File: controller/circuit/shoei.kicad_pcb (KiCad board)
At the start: 2 copper layers, 68.6 x 53.3 mm, 28 parts, among them J1 LED1, J2 LED2, J3 LED3, J4 LED-Sensor, J5 12V, J6 Sensor-In, J7 VL53L0X, J8 SPEAKER, P1 Power, P2 Analog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

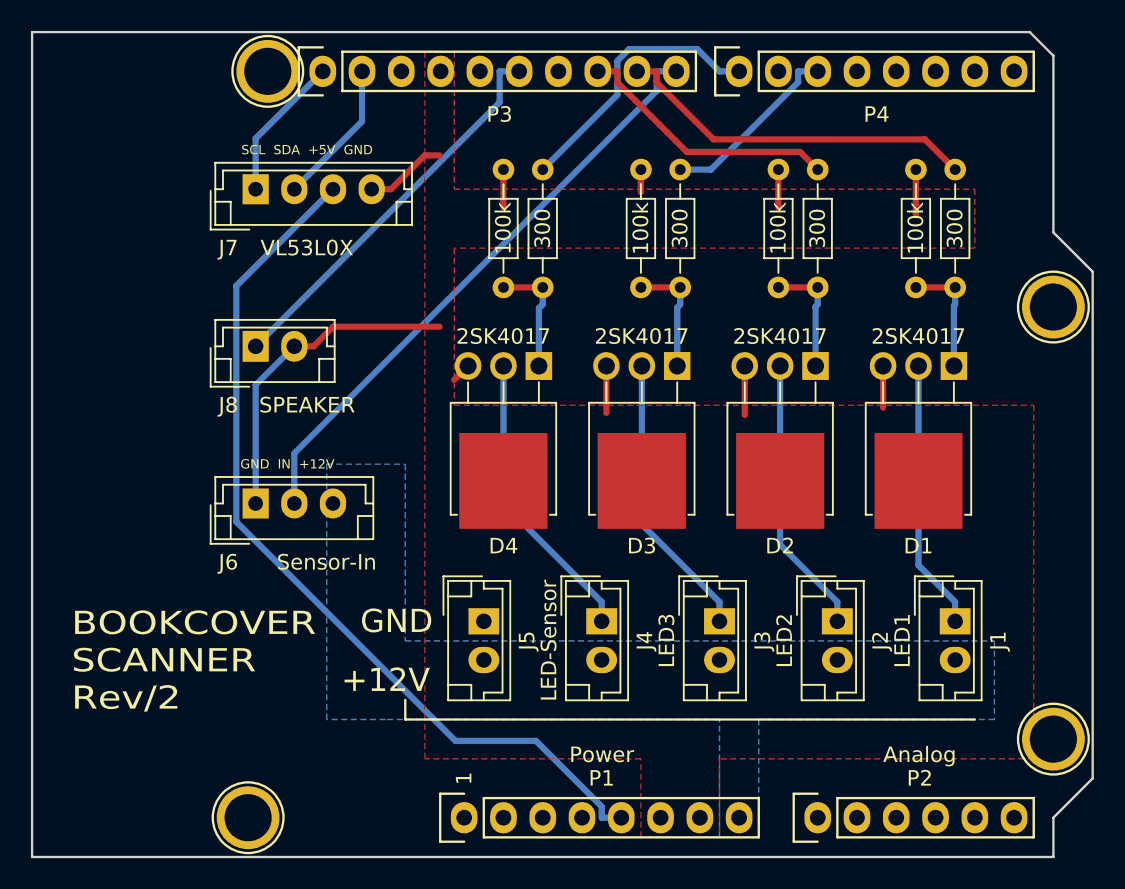
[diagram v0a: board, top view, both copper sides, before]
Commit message: update pcb silk
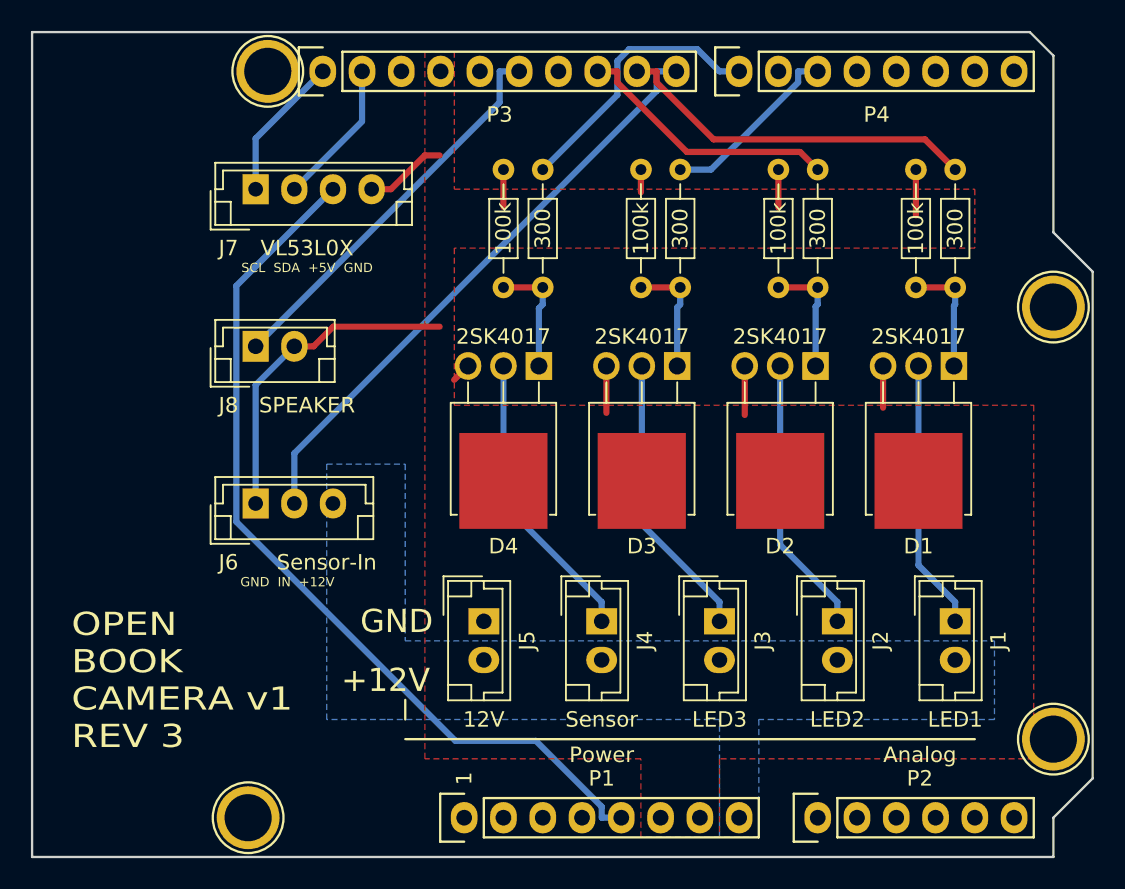
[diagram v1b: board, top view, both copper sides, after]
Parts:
- J4: value LED-Sensor -> Sensor
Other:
- board text added: "OPEN BOOK CAMERA v1 REV 3"
- board text removed: "BOOKCOVER SCANNER Rev/2"
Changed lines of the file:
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@@
   (general
     (thickness 1.6)
-    (drawings 40)
+    (drawings 39)
     (tracks 82)
     (zones 0)
@@
       (effects (font (size 1 1) (thickness 0.15)))
     )
-    (fp_text value LED2 (at 1.25 3.4 270) (layer F.SilkS)
+    (fp_text value LED2 (at 6.35 0 180) (layer F.SilkS)
       (effects (font (size 1 1) (thickness 0.15)))
     )
@@
       (effects (font (size 1 1) (thickness 0.15)))
     )
-    (fp_text value LED3 (at 1.25 3.4 270) (layer F.SilkS)
+    (fp_text value LED3 (at 6.35 0) (layer F.SilkS)
       (effects (font (size 1 1) (thickness 0.15)))
     )
@@
       (effects (font (size 1 1) (thickness 0.15)))
     )
-    (fp_text value LED-Sensor (at 1.25 3.4 270) (layer F.SilkS)
+    (fp_text value Sensor (at 6.35 0 180) (layer F.SilkS)
       (effects (font (size 1 1) (thickness 0.15)))
     )
@@
       (effects (font (size 1 1) (thickness 0.15)))
     )
-    (fp_text value 12V (at 1.25 3.4 270) (layer F.Fab)
+    (fp_text value 12V (at 6.35 0 180) (layer F.SilkS)
       (effects (font (size 1 1) (thickness 0.15)))
     )
@@
       (effects (font (size 1 1) (thickness 0.15)))
     )
-    (fp_text value LED1 (at 1.25 3.4 270) (layer F.SilkS)
+    (fp_text value LED1 (at 6.35 0 180) (layer F.SilkS)
       (effects (font (size 1 1) (thickness 0.15)))
     )
@@
       (net 25 "Net-(P8-Pad1)"))
   )
-  (gr_text "BOOKCOVER\nSCANNER\nRev/2" (at 113.538 113.665) (layer F.SilkS)
+  (gr_text "OPEN \nBOOK\nCAMERA v1 \nREV 3" (at 113.538 114.935) (layer F.SilkS)
     (effects (font (size 1.5 1.8) (thickness 0.3)) (justify left))
   )
-  (gr_line (start 135.128 117.475) (end 171.958 117.475) (layer F.SilkS) (width 0.15))
+  (gr_line (start 135.128 118.745) (end 171.958 118.745) (layer F.SilkS) (width 0.15))
   (gr_line (start 135.128 116.205) (end 135.128 117.475) (layer F.SilkS) (width 0.15))
   (gr_line (start 135.128 117.475) (end 135.128 118.745) (layer F.Fab) (width 0.15))
@@
     (effects (font (size 1.5 1.5) (thickness 0.3)))
   )
-  (gr_text GND (at 130.048 116.205) (layer F.Fab)
-    (effects (font (size 1.5 1.5) (thickness 0.3)))
-  )
   (gr_text +12V (at 133.858 114.935) (layer F.SilkS)
     (effects (font (size 1.5 1.5) (thickness 0.3)))
   )
-  (gr_text "GND  IN  +12V" (at 127.508 100.965) (layer F.SilkS)
+  (gr_text "GND  IN  +12V" (at 127.508 108.585) (layer F.SilkS)
     (effects (font (size 0.6 0.6) (thickness 0.09)))
   )
-  (gr_text "SCL  SDA  +5V  GND" (at 128.778 80.645) (layer F.SilkS)
+  (gr_text "SCL  SDA  +5V  GND" (at 128.778 88.265) (layer F.SilkS)
     (effects (font (size 0.6 0.6) (thickness 0.09)))
   )
